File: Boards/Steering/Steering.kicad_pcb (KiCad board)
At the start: 2 copper layers, 68.6 x 20.3 mm, 25 parts, among them J1 NanoFit_RA_02, J2 NanoFit_RA_04, J3 NanoFit_RA_06, J4 CONN_02X03, U1 MCP2561-E_SN, U2 MICROCONTROLLER, Y1 Crystal_SMD

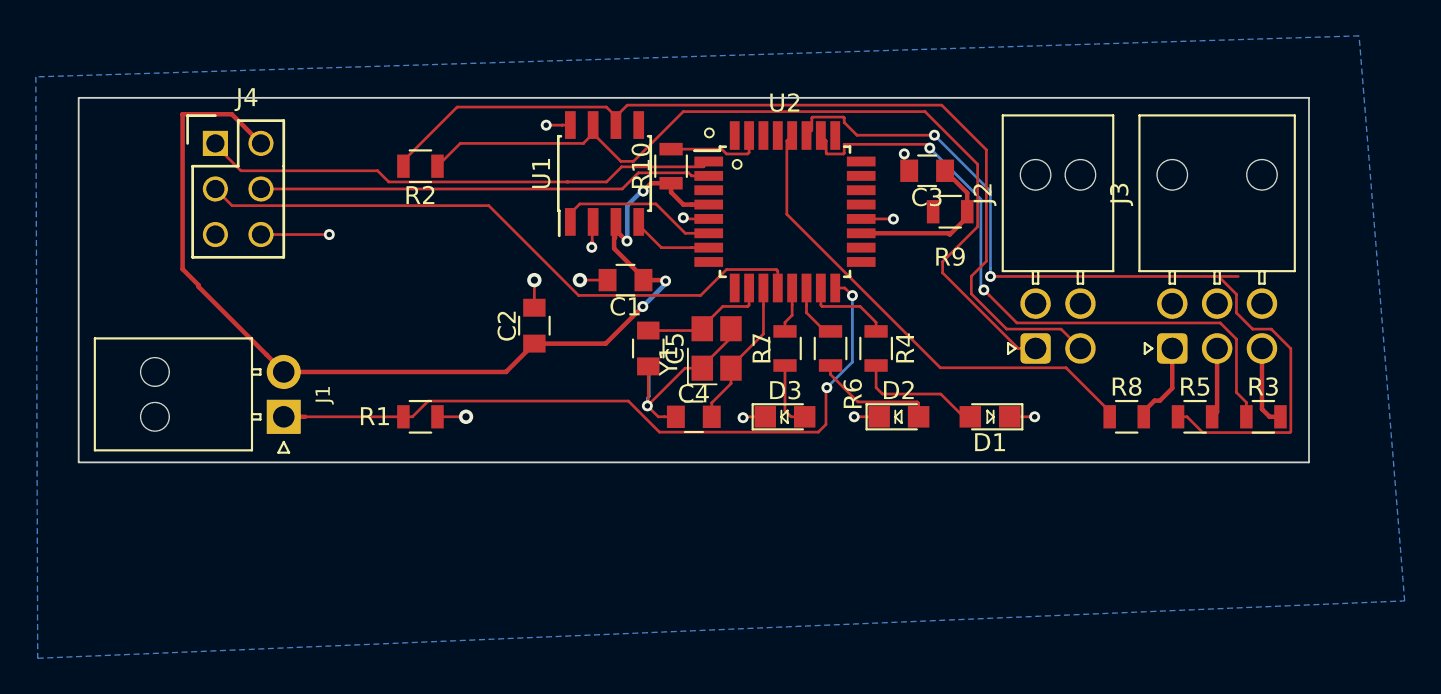
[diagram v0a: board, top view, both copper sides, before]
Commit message: Fixed VCC & CAN Traces. Added Name Silkscreen
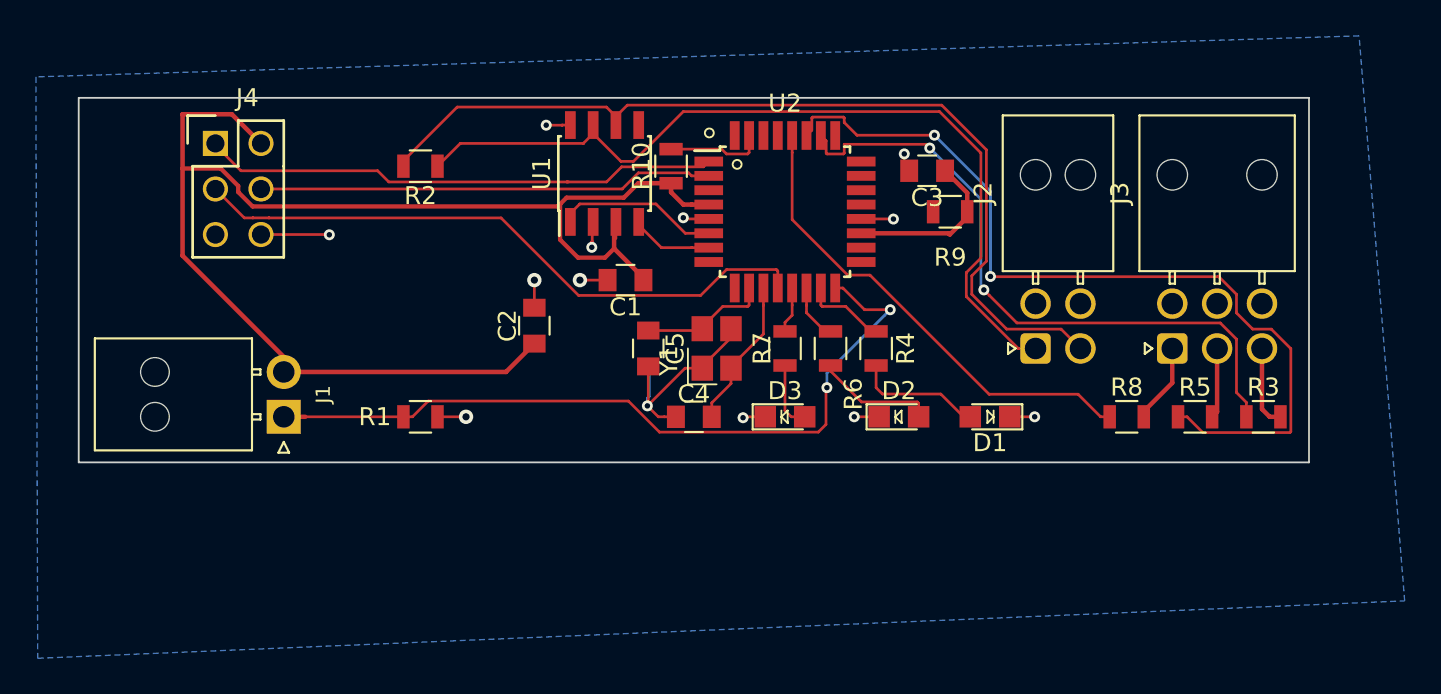
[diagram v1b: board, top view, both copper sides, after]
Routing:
- net VCC: track 60.7 -> 79.0 mm, vias 4 -> 0
- net /B1_In: track 40.4 -> 42.9 mm
- net /LED_Driver2: track 49.1 -> 48.0 mm
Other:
- board text added: "Oscar Delagarza Steering Board Rev 1 | 12.15 OEM - MKV"
